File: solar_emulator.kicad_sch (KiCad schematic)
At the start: 80 parts, among them J1 USB_C_Receptacle_USB2.0_16P, J2 Conn_01x02, J3 Conn_01x02, J4 Conn_01x02, J5 Conn_01x02, J6 Conn_01x03, J7 Conn_01x04, Q1 IRFZ44N, Q2 IRFZ44N, Q3 IRFZ44N, Q4 IRFZ44N, Q5 IRFZ44N, Q6 IRFZ44N, Q7 IRFZ44N, Q8 IRFZ44N, SW1 SW_Push, SW2 SW_Push, U1 ESP32-S3-WROOM-1, U2 LD1117S33TR_SOT223, U3 HIP4081AIPZ, U4 HIP4081AIPZ, U5 LM393, U6 LM393, U7 USBLC6-2SC6

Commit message: tracing complete, need to optimize pcb
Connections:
- net AHI1: now also U1.21 (GPIO13/TOUCH13/ADC2_CH2/FSPIQ/FSPIIO7/SUBSPIQ); no longer U1.23 (GPIO21)
- net AHI2: now also U1.17 (GPIO9/TOUCH9/ADC1_CH8/FSPIHD/SUBSPIHD); no longer U1.15 (GPIO3/TOUCH3/ADC1_CH2)
- net ALI1: now also U1.22 (GPIO14/TOUCH14/ADC2_CH3/FSPIWP/FSPIDQS/SUBSPIWP); no longer U1.24 (GPIO47/SPICLK_P/SUBSPICLK_P_DIFF)
- net ALI2: now also U1.18 (GPIO10/TOUCH10/ADC1_CH9/FSPICS0/FSPIIO4/SUBSPICS0); no longer U1.16 (GPIO46)
- net BHI1: now also U1.24 (GPIO47/SPICLK_P/SUBSPICLK_P_DIFF); no longer U1.26 (GPIO45)
- net BHI2: now also U1.20 (GPIO12/TOUCH12/ADC2_CH1/FSPICLK/FSPIIO6/SUBSPICLK); no longer U1.18 (GPIO10/TOUCH10/ADC1_CH9/FSPICS0/FSPIIO4/SUBSPICS0)
- net BLI1: now also U1.23 (GPIO21); no longer U1.25 (GPIO48/SPICLK_N/SUBSPICLK_N_DIFF)
- net BLI2: now also U1.19 (GPIO11/TOUCH11/ADC2_CH0/FSPID/FSPIIO5/SUBSPID); no longer U1.17 (GPIO9/TOUCH9/ADC1_CH8/FSPIHD/SUBSPIHD)
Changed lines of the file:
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@@
 	)
 	(no_connect
-		(at 118.11 69.85)
+		(at 118.11 49.53)
 	)
 	(no_connect
@@
 	)
 	(no_connect
-		(at 118.11 77.47)
+		(at 118.11 90.17)
 	)
 	(no_connect
@@
 	)
 	(no_connect
-		(at 118.11 74.93)
+		(at 118.11 97.79)
 	)
 	(no_connect
-		(at 118.11 72.39)
+		(at 118.11 92.71)
 	)
 	(no_connect
@@
 	(global_label "BHI2"
 		(shape input)
-		(at 118.11 67.31 0)
+		(at 118.11 72.39 0)
 		(fields_autoplaced yes)
 		(effects
@@
 		)
 		(property "Intersheetrefs" "${INTERSHEET_REFS}"
-			(at 125.51 67.31 0)
+			(at 125.51 72.39 0)
 			(hide yes)
 			(show_name no)
@@
 	(global_label "ALI2"
 		(shape input)
-		(at 118.11 92.71 0)
+		(at 118.11 67.31 0)
 		(fields_autoplaced yes)
 		(effects
@@
 		)
 		(property "Intersheetrefs" "${INTERSHEET_REFS}"
-			(at 125.0262 92.71 0)
+			(at 125.0262 67.31 0)
 			(hide yes)
 			(show_name no)
@@
 	(global_label "BLI2"
 		(shape input)
-		(at 118.11 64.77 0)
+		(at 118.11 69.85 0)
 		(fields_autoplaced yes)
 		(effects
@@
 		)
 		(property "Intersheetrefs" "${INTERSHEET_REFS}"
-			(at 125.2076 64.77 0)
+			(at 125.2076 69.85 0)
 			(hide yes)
 			(show_name no)
@@
 	(global_label "BLI1"
 		(shape input)
-		(at 118.11 97.79 0)
+		(at 118.11 85.09 0)
 		(fields_autoplaced yes)
 		(effects
@@
 		)
 		(property "Intersheetrefs" "${INTERSHEET_REFS}"
-			(at 126.9614 97.79 0)
+			(at 126.9614 85.09 0)
 			(hide yes)
 			(show_name no)
@@
 	(global_label "AHI2"
 		(shape input)
-		(at 118.11 49.53 0)
+		(at 118.11 64.77 0)
 		(fields_autoplaced yes)
 		(effects
@@
 		)
 		(property "Intersheetrefs" "${INTERSHEET_REFS}"
-			(at 125.3286 49.53 0)
+			(at 125.3286 64.77 0)
 			(hide yes)
 			(show_name no)
@@
 	(global_label "AHI1"
 		(shape input)
-		(at 118.11 85.09 0)
+		(at 118.11 74.93 0)
 		(fields_autoplaced yes)
 		(effects
@@
 		)
 		(property "Intersheetrefs" "${INTERSHEET_REFS}"
-			(at 125.3286 85.09 0)
+			(at 125.3286 74.93 0)
 			(hide yes)
 			(show_name no)
@@
 	(global_label "ALI1"
 		(shape input)
-		(at 118.11 95.25 0)
+		(at 118.11 77.47 0)
 		(fields_autoplaced yes)
 		(effects
@@
 		)
 		(property "Intersheetrefs" "${INTERSHEET_REFS}"
-			(at 125.0262 95.25 0)
+			(at 125.0262 77.47 0)
 			(hide yes)
 			(show_name no)
@@
 	(global_label "BHI1"
 		(shape input)
-		(at 118.11 90.17 0)
+		(at 118.11 95.25 0)
 		(fields_autoplaced yes)
 		(effects
@@
 		)
 		(property "Intersheetrefs" "${INTERSHEET_REFS}"
-			(at 126.9614 90.17 0)
+			(at 126.9614 95.25 0)
 			(hide yes)
 			(show_name no)

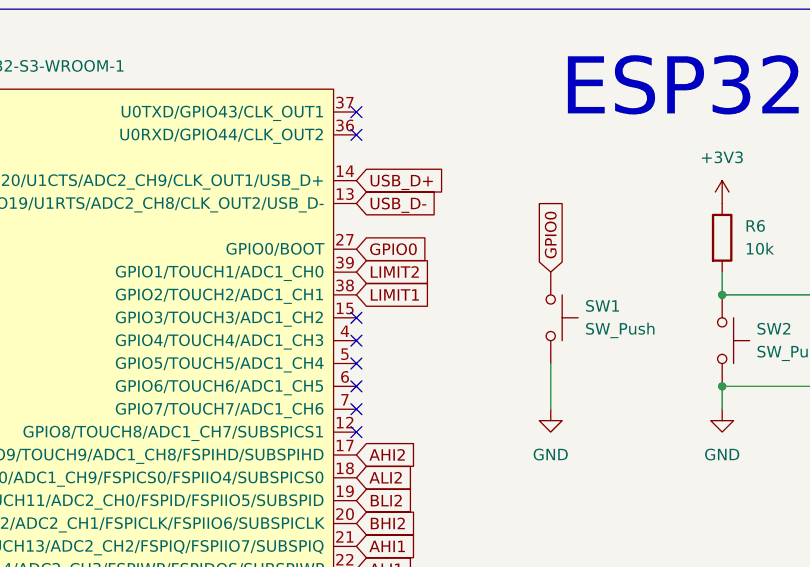
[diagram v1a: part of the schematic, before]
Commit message: rearrange connectors, traces, add via stitching
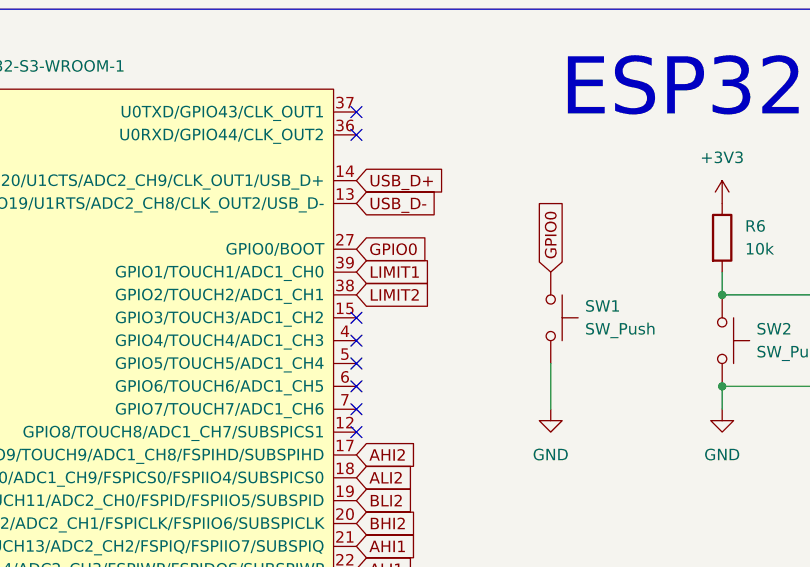
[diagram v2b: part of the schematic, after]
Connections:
- net LIMIT1: now also U1.39 (GPIO1/TOUCH1/ADC1_CH0); no longer U1.38 (GPIO2/TOUCH2/ADC1_CH1)
- net LIMIT2: now also U1.38 (GPIO2/TOUCH2/ADC1_CH1); no longer U1.39 (GPIO1/TOUCH1/ADC1_CH0)
